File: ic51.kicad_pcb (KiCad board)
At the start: 2 copper layers, 5 parts, among them J1 Conn_02x18_Odd_Even, J2 Conn_02x18_Odd_Even, J3 Conn_02x18_Odd_Even, J4 Conn_02x18_Odd_Even, U1 ic51-1444-schem

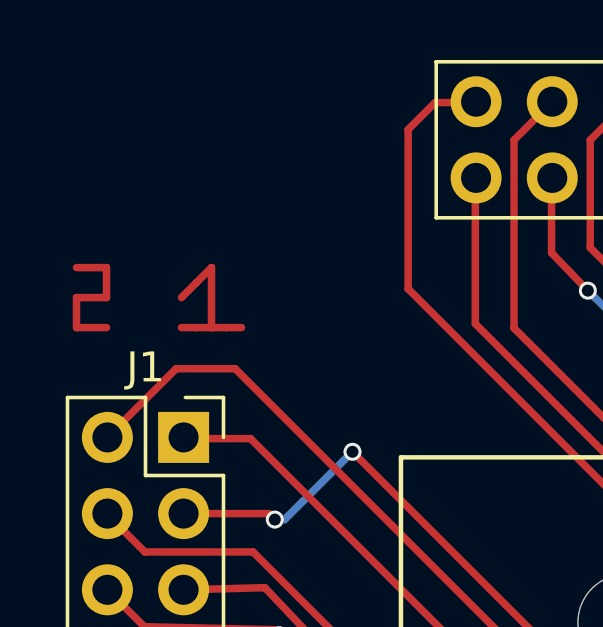
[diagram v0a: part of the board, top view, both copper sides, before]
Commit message: added number indicator in top cu layer
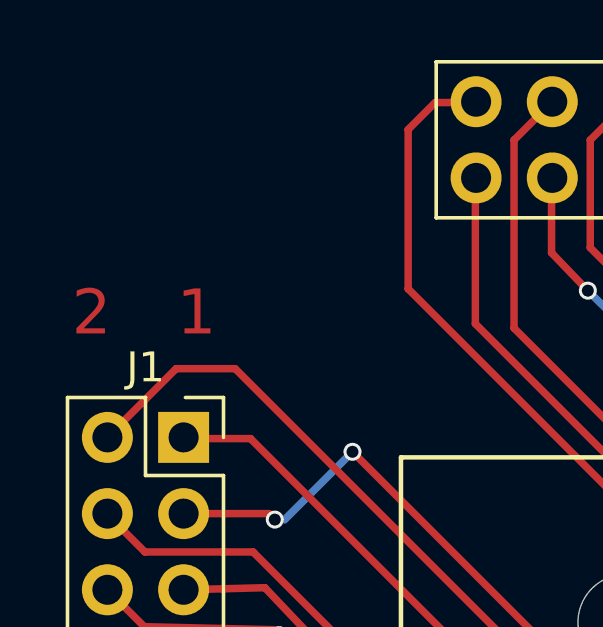
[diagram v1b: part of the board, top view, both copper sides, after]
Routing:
- net (no net): track 10.4 -> 0.00 mm
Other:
- board text added: "1"
- board text added: "2"
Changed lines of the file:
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@@
     (area 105.647618 52.997618 186.912382 134.382382)
     (thickness 1.6)
-    (drawings 4)
-    (tracks 1148)
+    (drawings 6)
+    (tracks 1136)
     (zones 0)
     (modules 5)
@@
     )
   )
+  (gr_text 2 (at 112.5 67.5) (layer F.Cu)
+    (effects (font (size 1.5 1.5) (thickness 0.3)))
+  )
+  (gr_text 1 (at 116 67.5) (layer F.Cu)
+    (effects (font (size 1.5 1.5) (thickness 0.3)))
+  )
   (gr_line (start 107.96 56.27) (end 184.71 56.27) (angle 90) (layer Eco1.User) (width 0.2))
   (gr_line (start 107.95 132.08) (end 107.95 56.18) (angle 90) (layer Eco1.User) (width 0.2))
   (gr_line (start 184.66 132.08) (end 107.95 132.08) (angle 90) (layer Eco1.User) (width 0.2))
   (gr_line (start 184.66 56.18) (end 184.66 132.08) (angle 90) (layer Eco1.User) (width 0.2))
-  (segment (start 115.5 68) (end 116 68) (width 0.25) (layer F.Cu) (net 0))
-  (segment (start 116 68) (end 116.5 68) (width 0.25) (layer F.Cu) (net 0))
-  (segment (start 117.5 68) (end 117 68) (width 0.25) (layer F.Cu) (net 0))
-  (segment (start 117 68) (end 116.5 68) (width 0.25) (layer F.Cu) (net 0))
-  (segment (start 115.5 67) (end 116 66.5) (width 0.25) (layer F.Cu) (net 0))
-  (segment (start 116.5 66) (end 116.5 68) (width 0.25) (layer F.Cu) (net 0))
-  (segment (start 116 66.5) (end 116.5 66) (width 0.25) (layer F.Cu) (net 0))
-  (segment (start 112 66) (end 113 66) (width 0.25) (layer F.Cu) (net 0))
-  (segment (start 112 68) (end 113 68) (width 0.25) (layer F.Cu) (net 0))
-  (segment (start 112 67) (end 112 68) (width 0.25) (layer F.Cu) (net 0))
-  (segment (start 113 67) (end 112 67) (width 0.25) (layer F.Cu) (net 0))
-  (segment (start 113 66) (end 113 67) (width 0.25) (layer F.Cu) (net 0))
   (segment (start 115.61 71.7) (end 117.8 71.7) (width 0.25) (layer F.Cu) (net 1))
   (segment (start 129.735001 83.635001) (end 129.735001 85.7625) (width 0.25) (layer F.Cu) (net 1))

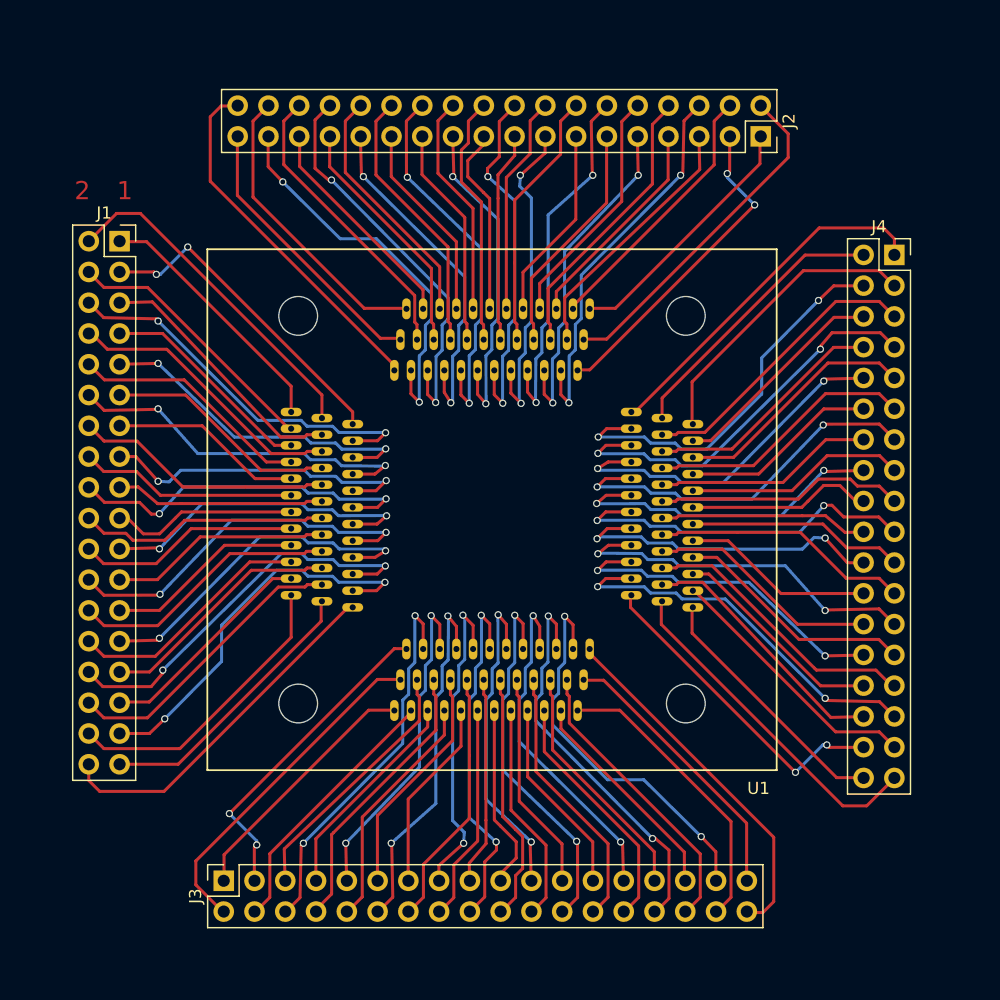
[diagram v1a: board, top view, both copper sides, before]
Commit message: name all the port in silk layer
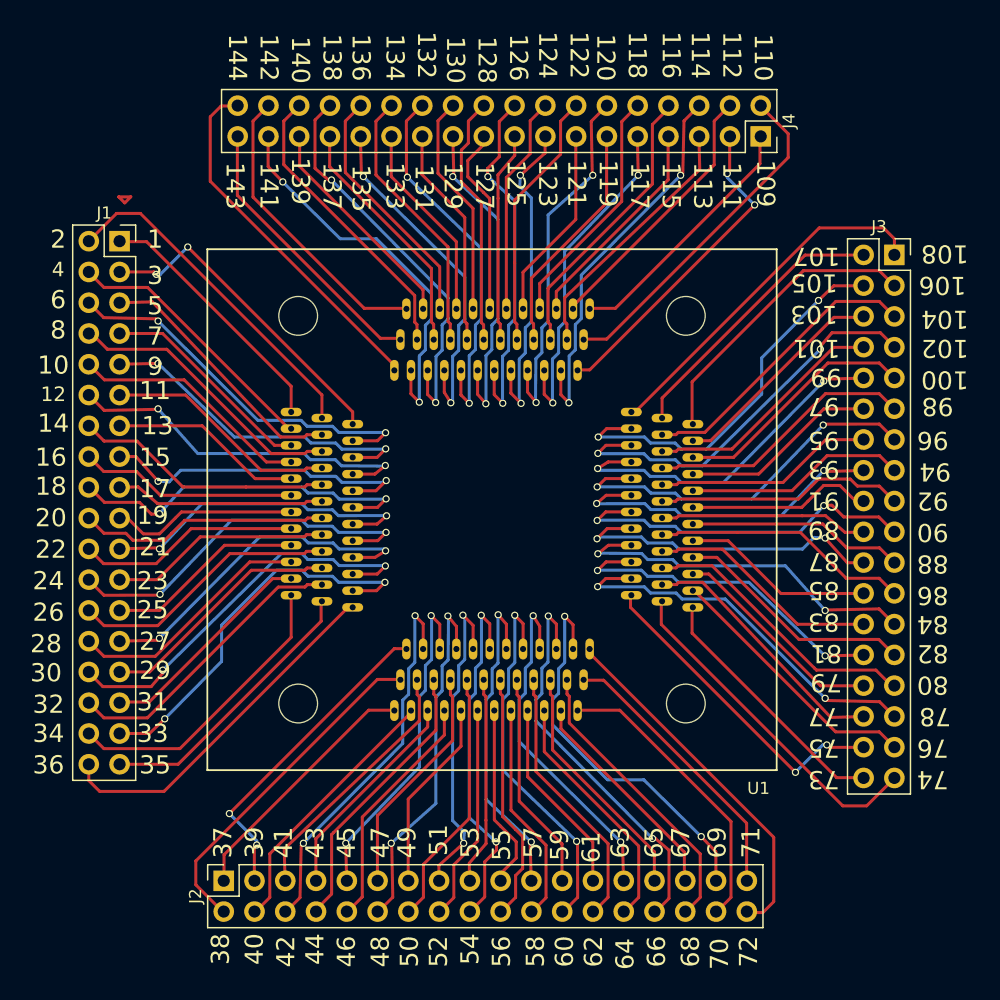
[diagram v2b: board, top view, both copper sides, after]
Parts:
- renumbered J3 to J2, J4 to J3, J2 to J4
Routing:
- net (no net): track 0.00 -> 2.41 mm
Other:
- board text added: "10"
- board text added: "100"
- board text added: "101"
- board text added: "102"
- board text added: "103"
- board text added: "104"
- board text added: "105"
- board text added: "106"
- board text added: "107"
- board text added: "108"
- board text added: "109"
- board text added: "11"
- board text added: "110"
- board text added: "111"
- board text added: "112"
- board text added: "113"
- board text added: "114"
- board text added: "115"
- board text added: "116"
- board text added: "117"
- board text added: "118"
- board text added: "119"
- board text added: "12"
- board text added: "120"
- board text added: "121"
- board text added: "122"
- board text added: "123"
- board text added: "124"
- board text added: "125"
- board text added: "126"
- board text added: "127"
- board text added: "128"
- board text added: "129"
- board text added: "13"
- board text added: "130"
- board text added: "131"
- board text added: "132"
- board text added: "133"
- board text added: "134"
- board text added: "135"
- board text added: "136"
- board text added: "137"
- board text added: "138"
- board text added: "139"
- board text added: "14"
- board text added: "140"
- board text added: "141"
- board text added: "142"
- board text added: "143"
- board text added: "144"
- board text added: "15"
- board text added: "16"
- board text added: "17"
- board text added: "18"
- board text added: "19"
- board text added: "20"
- board text added: "21"
- board text added: "22"
- board text added: "23"
- board text added: "24"
- board text added: "25"
- board text added: "26"
- board text added: "27"
- board text added: "28"
- board text added: "29"
- board text added: "3"
- board text added: "30"
- board text added: "31"
- board text added: "32"
- board text added: "33"
- board text added: "34"
- board text added: "35"
- board text added: "36"
- board text added: "37"
- board text added: "38"
- board text added: "39"
- board text added: "4"
- board text added: "40"
- board text added: "41"
- board text added: "42"
- board text added: "43"
- board text added: "44"
- board text added: "45"
- board text added: "46"
- board text added: "47"
- board text added: "48"
- board text added: "49"
- board text added: "5"
- board text added: "50"
- board text added: "51"
- board text added: "52"
- board text added: "53"
- board text added: "54"
- board text added: "55"
- board text added: "56"
- board text added: "57"
- board text added: "58"
- board text added: "59"
- board text added: "6"
- board text added: "60"
- board text added: "61"
- board text added: "62"
- board text added: "63"
- board text added: "64"
- board text added: "65"
- board text added: "66"
- board text added: "67"
- board text added: "68"
- board text added: "69"
- board text added: "7"
- board text added: "70"
- board text added: "71"
- board text added: "72"
- board text added: "73"
- board text added: "74"
- board text added: "75"
- board text added: "76"
- board text added: "77"
- board text added: "78"
- board text added: "79"
- board text added: "8"
- board text added: "80"
- board text added: "81"
- board text added: "82"
- board text added: "83"
- board text added: "84"
- board text added: "85"
- board text added: "86"
- board text added: "87"
- board text added: "88"
- board text added: "89"
- board text added: "9"
- board text added: "90"
- board text added: "91"
- board text added: "92"
- board text added: "93"
- board text added: "94"
- board text added: "95"
- board text added: "96"
- board text added: "97"
- board text added: "98"
- board text added: "99"

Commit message: ready for pcb-house
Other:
- net class Default: via_dia 0.6 -> 1
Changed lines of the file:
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@@
     (segment_width 0.2)
     (edge_width 0.15)
-    (via_size 0.6)
+    (via_size 1)
     (via_drill 0.4)
     (via_min_size 0.4)
@@
     (clearance 0.2)
     (trace_width 0.25)
-    (via_dia 0.6)
+    (via_dia 1)
     (via_drill 0.4)
     (uvia_dia 0.3)

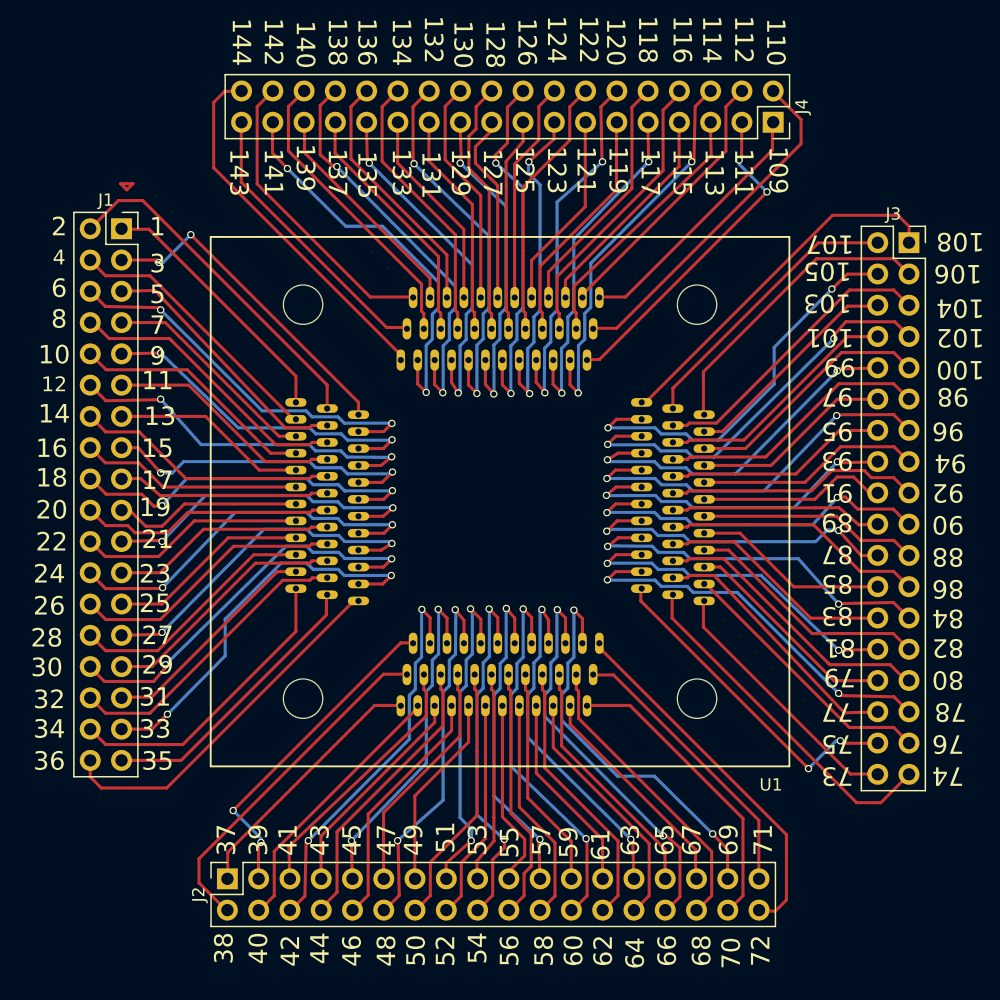
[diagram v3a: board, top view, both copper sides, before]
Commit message: fixed the pin header location
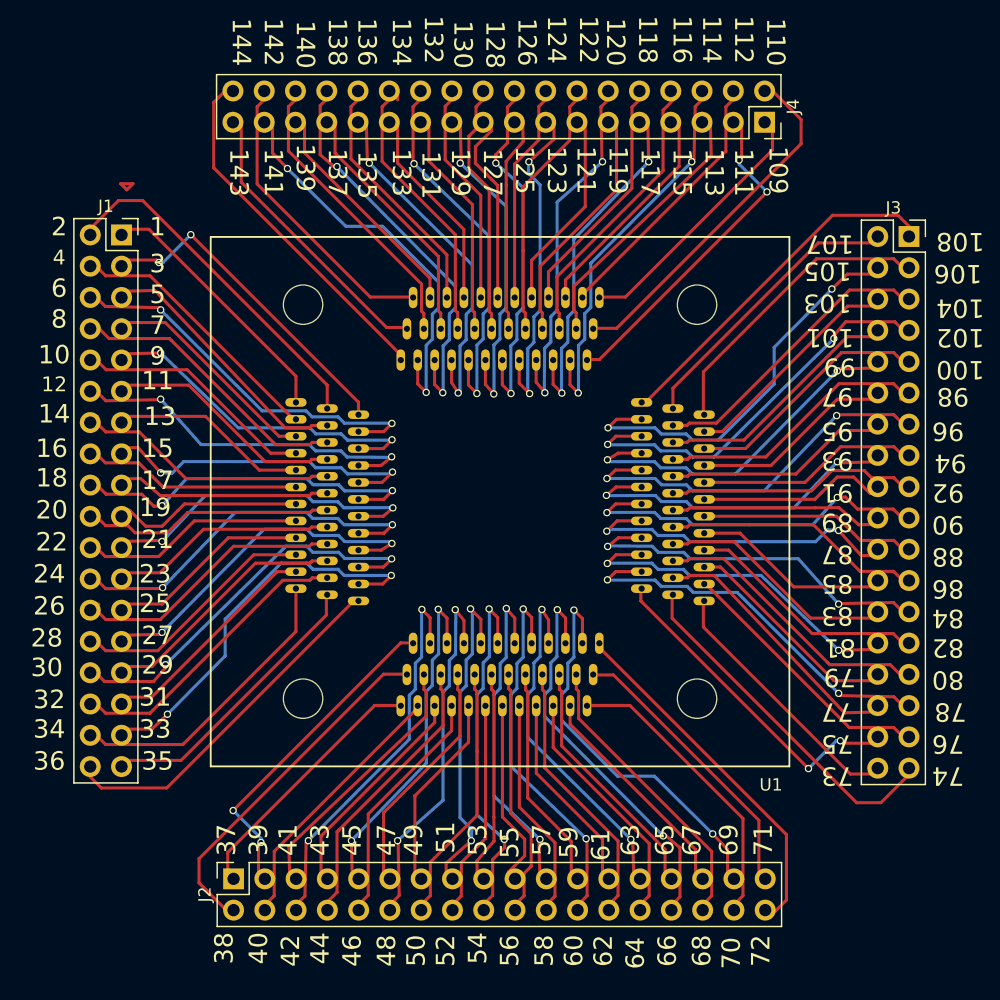
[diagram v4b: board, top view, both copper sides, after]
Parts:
- moved J4 0.70 mm to (167.8, 63.0)
- moved J1 0.50 mm to (115.6, 72.2)
- moved J2 0.50 mm to (124.7, 124.5)
- moved J3 0.50 mm to (179.5, 72.3)
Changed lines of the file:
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@@
     (add_net /99)
   )
-  (module ic51-1444:ic51-1444-footprint (layer F.Cu)
+  (module ic51-1444:ic51-1444-footprint locked (layer F.Cu)
     (at 146.315001 93.825)
     (fp_text reference U1 (at 22 23) (layer F.SilkS)
@@
     (pad "" np_thru_hole circle (at -16 -16) (size 3.2 3.2) (drill 3.2) (layers *.Cu *.Mask))
   )
-  (module Socket_Strips:Socket_Strip_Straight_2x18_Pitch2.54mm (layer F.Cu)
-    (at 115.57 71.66)
+  (module Socket_Strips:Socket_Strip_Straight_2x18_Pitch2.54mm locked (layer F.Cu)
+    (at 115.57 72.16)
     (descr "Through hole straight socket strip, 2x18, 2.54mm pitch, double rows")
     (tags "Through hole socket strip THT 2x18 2.54mm double row")
@@
     )
   )
-  (module Socket_Strips:Socket_Strip_Straight_2x18_Pitch2.54mm (layer F.Cu)
-    (at 168.5 63.01 270)
+  (module Socket_Strips:Socket_Strip_Straight_2x18_Pitch2.54mm locked (layer F.Cu)
+    (at 167.8 63.01 270)
     (descr "Through hole straight socket strip, 2x18, 2.54mm pitch, double rows")
     (tags "Through hole socket strip THT 2x18 2.54mm double row")
@@
     )
   )
-  (module Socket_Strips:Socket_Strip_Straight_2x18_Pitch2.54mm (layer F.Cu)
-    (at 124.17 124.46 90)
+  (module Socket_Strips:Socket_Strip_Straight_2x18_Pitch2.54mm locked (layer F.Cu)
+    (at 124.67 124.46 90)
     (descr "Through hole straight socket strip, 2x18, 2.54mm pitch, double rows")
     (tags "Through hole socket strip THT 2x18 2.54mm double row")
@@
     )
   )
-  (module Socket_Strips:Socket_Strip_Straight_2x18_Pitch2.54mm (layer F.Cu)
-    (at 179.53 72.79)
+  (module Socket_Strips:Socket_Strip_Straight_2x18_Pitch2.54mm locked (layer F.Cu)
+    (at 179.53 72.29)
     (descr "Through hole straight socket strip, 2x18, 2.54mm pitch, double rows")
     (tags "Through hole socket strip THT 2x18 2.54mm double row")

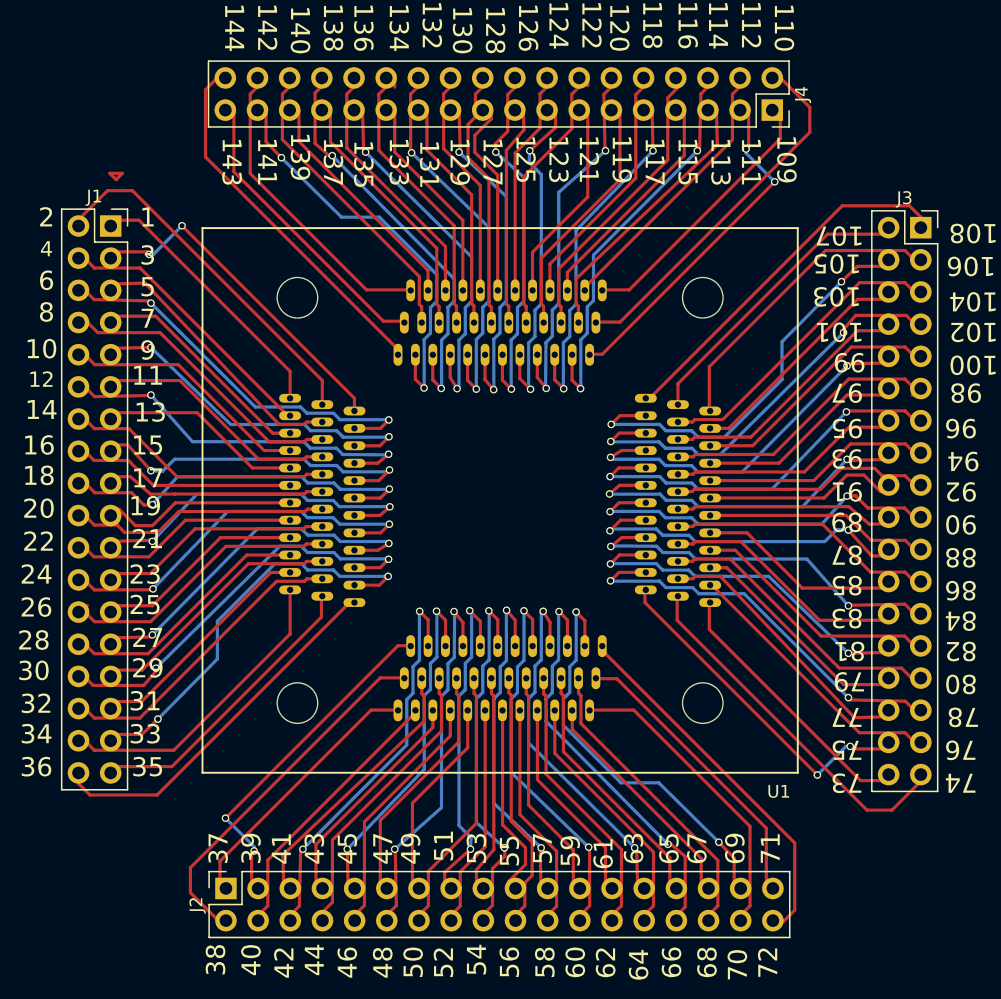
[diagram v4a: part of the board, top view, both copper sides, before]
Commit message: fixed all tracks to correspond to proper alignment
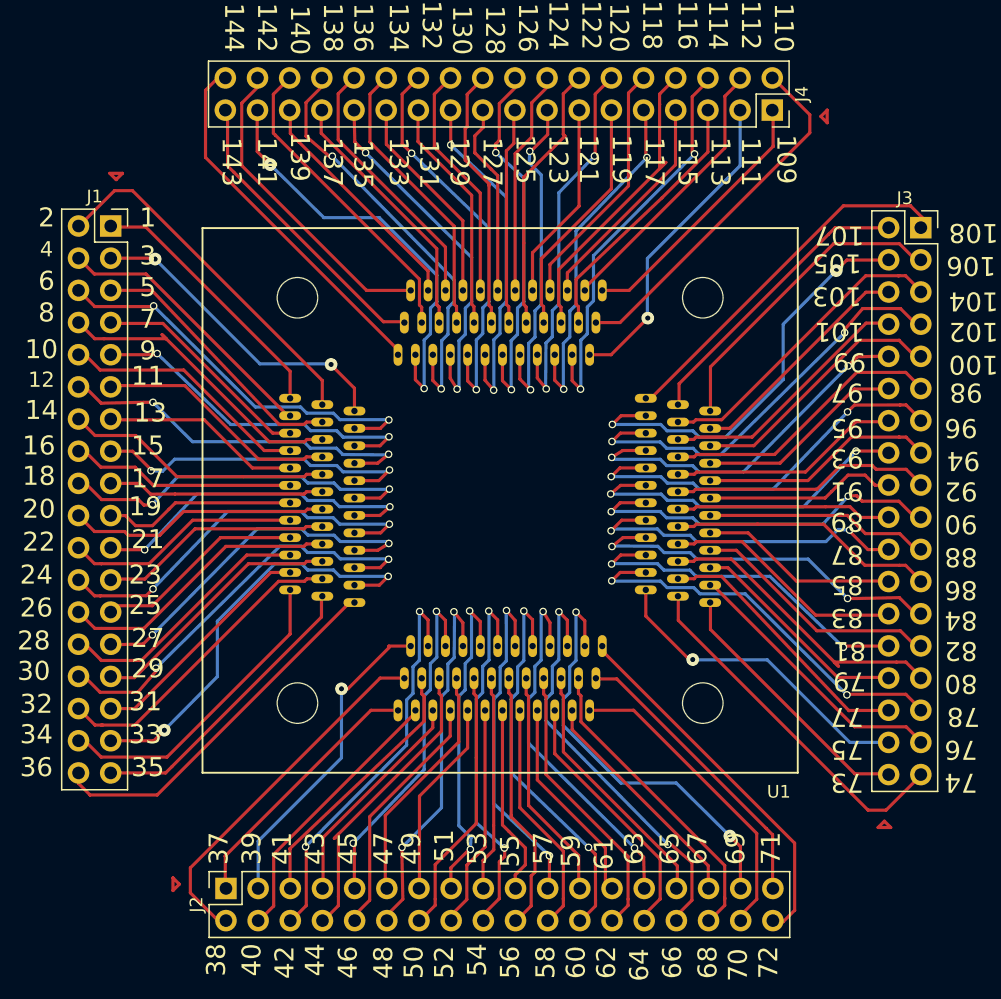
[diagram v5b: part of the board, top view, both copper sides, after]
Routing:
- net (no net): track 2.41 -> 9.66 mm
- net /111: track 26.9 -> 25.3 mm, vias 2 -> 1
- net /3: track 26.9 -> 25.3 mm
- net /75: track 26.9 -> 25.4 mm, vias 2 -> 1
- net /39: track 26.9 -> 25.4 mm, vias 2 -> 1
- net /116: track 24.0 -> 25.2 mm
- net /141: track 32.6 -> 33.7 mm
- net /69: track 32.6 -> 33.7 mm
- net /105: track 32.6 -> 33.7 mm
- net /33: track 32.6 -> 33.7 mm
- net /14: track 22.0 -> 21.2 mm
- net /86: track 22.0 -> 21.2 mm
- net /50: track 22.0 -> 21.2 mm
- net /80: track 24.0 -> 24.7 mm
- net /44: track 24.0 -> 24.7 mm
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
